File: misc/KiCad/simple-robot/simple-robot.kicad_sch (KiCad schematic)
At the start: 46 parts, among them J1 MotLA, J10 Screw_Terminal_2_P5.00mm, J2 MotLB, J4 MotRA, J5 MotRB, J6 ENC_LF, J7 ENC_LR, J8 ENC_RF, J9 ENC_RR, P1 Port Expander, U1 Pico2

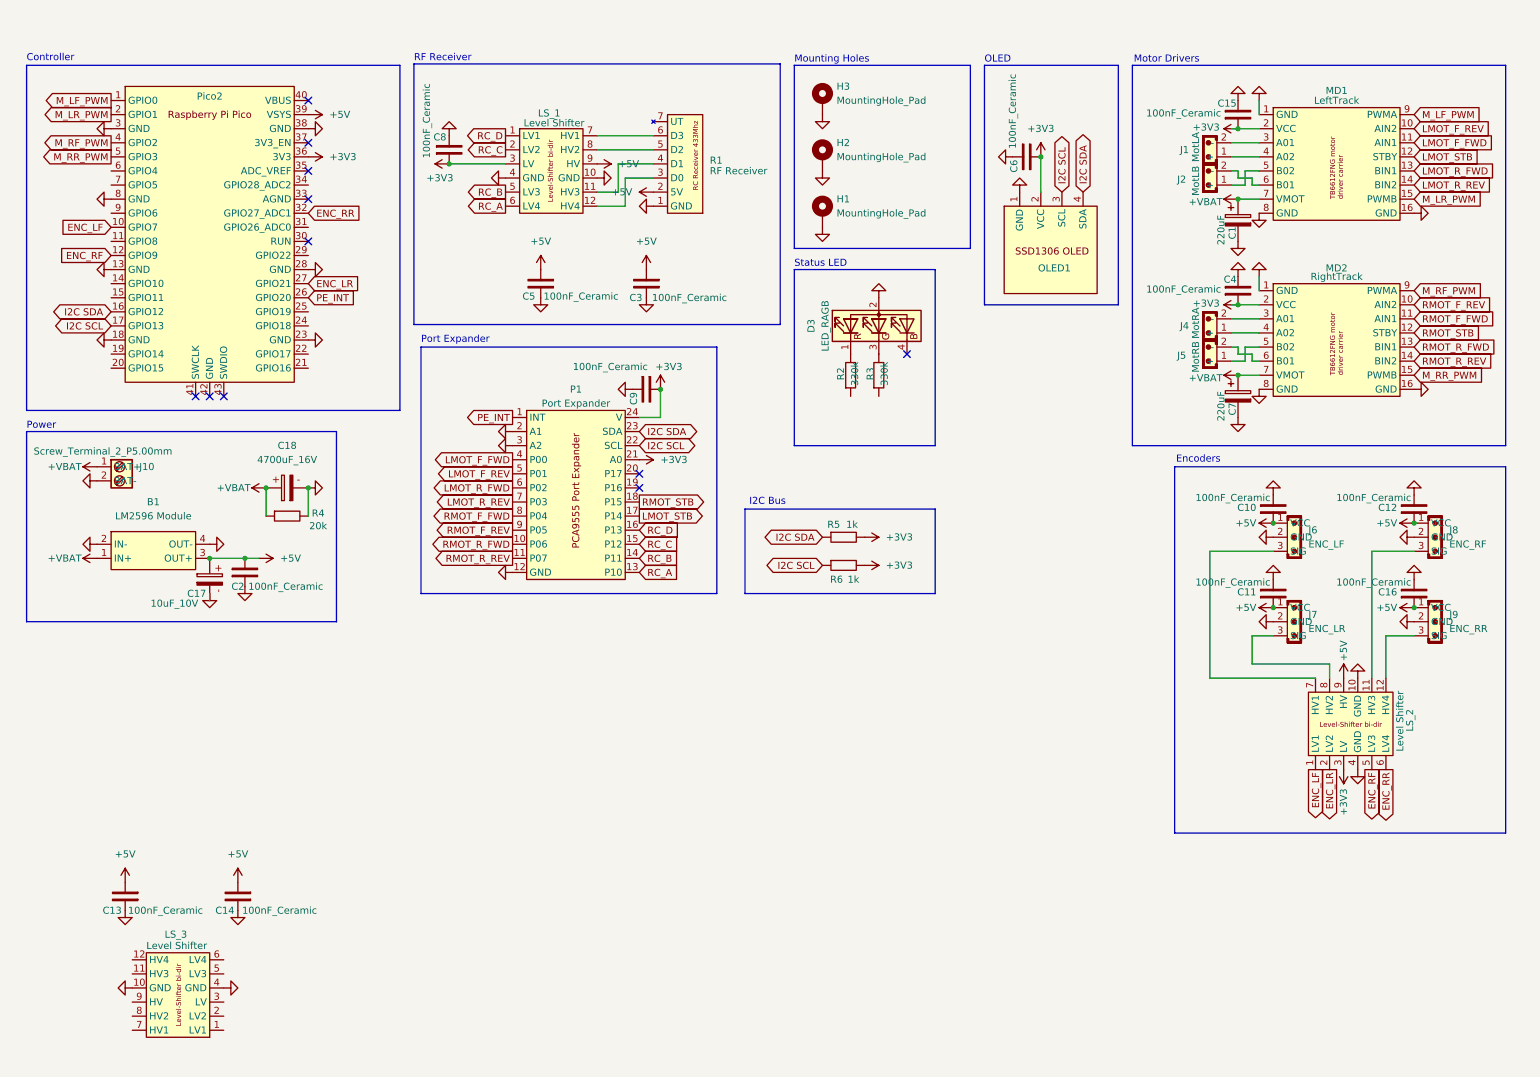
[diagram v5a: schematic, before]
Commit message: Update KiCad schematic to include all connections and IC
Make KiCad PCB 4-layer and update footprints
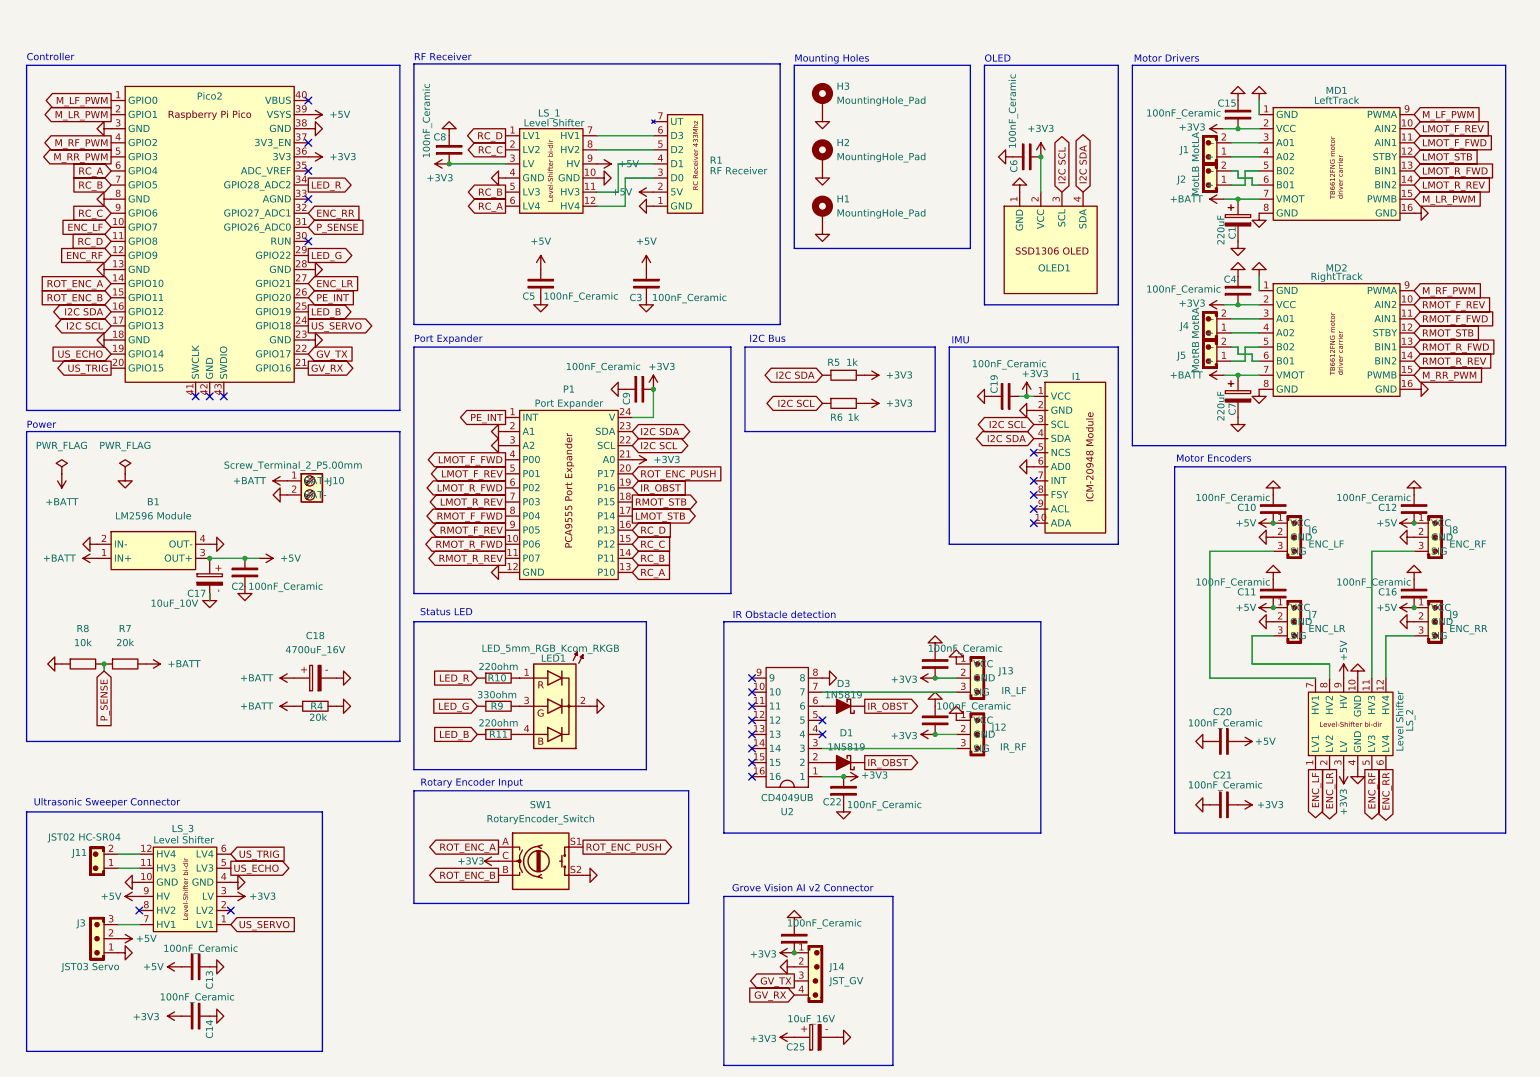
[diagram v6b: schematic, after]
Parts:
- removed D3: LED_RAGB, common-hobby-things:LED RAGB, symbol Device:LED_RAGB
- removed R2, R3: 330k, Resistor_THT:R_Axial_DIN0207_L6.3mm_D2.5mm_P10.16mm_Horizontal, symbol PCM_SL_Resistors:330k
- added C19, C20, C21, C22, C23, C24, C26: 100nF_Ceramic, Capacitor_THT:C_Disc_D5.0mm_W2.5mm_P2.50mm, symbol PCM_SL_Capacitors:100nF_Ceramic
- added C25: 10uF_16V, Capacitor_THT:CP_Radial_D5.0mm_P2.00mm, symbol PCM_SL_Capacitors:10uF_16V
- added D1, D3: 1N5819, PCM_Diode_THT_AKL:D_DO-41_SOD81_P7.62mm_Horizontal, symbol PCM_Diode_Schottky_AKL:1N5819
- added I1: ~, common-hobby-things:ICM-20948-module, symbol common-hobby-things:ICM-20948-module
- added J11: JST02 HC-SR04, Connector_JST:JST_EH_B2B-EH-A_1x02_P2.50mm_Vertical, symbol PCM_SL_Connectors:JST_02
- added J12: IR_RF, Connector_JST:JST_PH_B3B-PH-K_1x03_P2.00mm_Vertical, symbol PCM_SL_Connectors:JST_03
- added J13: IR_LF, Connector_JST:JST_PH_B3B-PH-K_1x03_P2.00mm_Vertical, symbol PCM_SL_Connectors:JST_03
- added J14: JST_GV, Connector_JST:JST_EH_B4B-EH-A_1x04_P2.50mm_Vertical, symbol PCM_SL_Connectors:JST_04
- added J3: JST03 Servo, Connector_JST:JST_EH_B3B-EH-A_1x03_P2.50mm_Vertical, symbol PCM_SL_Connectors:JST_03
- added LED1: LED_5mm_RGB_Kcom_RKGB, PCM_LED_THT_AKL:LED_D5.0mm-4_RGB_Wide_Pins, symbol PCM_LED_AKL:LED_5mm_RGB_Kcom_RKGB
- added R10, R11: 220ohm, Resistor_THT:R_Axial_DIN0207_L6.3mm_D2.5mm_P10.16mm_Horizontal, symbol PCM_SL_Resistors:220ohm
- added R7: 20k, Resistor_THT:R_Axial_DIN0207_L6.3mm_D2.5mm_P10.16mm_Horizontal, symbol PCM_SL_Resistors:20k
- added R8: 10k, Resistor_THT:R_Axial_DIN0207_L6.3mm_D2.5mm_P10.16mm_Horizontal, symbol PCM_SL_Resistors:10k
- added R9: 330ohm, Resistor_THT:R_Axial_DIN0207_L6.3mm_D2.5mm_P10.16mm_Horizontal, symbol PCM_SL_Resistors:330ohm
- added SW1: RotaryEncoder_Switch, Rotary_Encoder:RotaryEncoder_Alps_EC11E-Switch_Vertical_H20mm, symbol Device:RotaryEncoder_Switch
- added U2: CD4049UB, Package_DIP:DIP-16_W7.62mm_LongPads, symbol PCM_SL_Devices:IC_DIP_16
- U1: footprint MCU_RaspberryPi_and_Boards:RPi_Pico_SMD_TH -> PCM_SL_Development_Boards:raspberry_pi_pico_THT
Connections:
- net +3V3: now also C14.1, LS_3.3 (LV), C19.1, C21.2, C22.2, C23.1, C24.1, C25.1, C26.1, I1.1 (VCC), J12.2 (GND), J13.2 (GND), J14.1, SW1.C, U2.1
- net +5V: now also LS_3.9 (HV), C20.2, J3.2; no longer C14.1
- net GND: now also C19.2, C20.1, C21.1, C22.1, C23.2, C24.2, C25.2, C26.2, I1.2 (GND), I1.6 (AD0), J12.1 (VCC), J13.1 (VCC), J14.2, J3.1, LED1.2 (A), R8.1, SW1.S2, U2.8
- net I2C SCL: now also I1.3 (SCL)
- net I2C SDA: now also I1.4 (SDA)
- net RC_A: now also U1.6 (GPIO4)
- net RC_B: now also U1.7 (GPIO5)
- net RC_C: now also U1.9 (GPIO6)
- net RC_D: now also U1.11 (GPIO8)
- net US_SERVO: now reaches LS_3.1 (LV1)
- net US_SERVO: now also U1.24 (GPIO18)
- net at LS_3.11 (HV3): now also J11.1
- net at LS_3.12 (HV4): now also J11.2
- net US_ECHO: now reaches LS_3.5 (LV3)
- net US_ECHO: now also U1.19 (GPIO14)
- net US_TRIG: now reaches LS_3.6 (LV4)
- net US_TRIG: now also U1.20 (GPIO15)
- net at LS_3.7 (HV1): now also J3.3
- net IR_OBST: now reaches P1.19 (P16)
- net IR_OBST: now also D1.1 (K), D3.1 (K)
- net ROT_ENC_PUSH: now reaches P1.20 (P17)
- net ROT_ENC_PUSH: now also SW1.S1
- net ROT_ENC_A: now reaches U1.14 (GPIO10)
- net ROT_ENC_A: now also SW1.A
- net ROT_ENC_B: now reaches U1.15 (GPIO11)
- net ROT_ENC_B: now also SW1.B
- net GV_RX: now reaches U1.21 (GPIO16)
- net GV_RX: now also J14.4
- net GV_TX: now reaches U1.22 (GPIO17)
- net GV_TX: now also J14.3
- net LED_B: now reaches U1.25 (GPIO19)
- net LED_B: now also R11.1
- net LED_G: now reaches U1.29 (GPIO22)
- net LED_G: now also R9.1
- net P_SENSE: now reaches U1.31 (GPIO26_ADC0)
- net P_SENSE: now also R7.1, R8.2
- net LED_R: now reaches U1.34 (GPIO28_ADC2)
- net LED_R: now also R10.1
- net +VBAT renamed +BATT
- net +BATT: now also R7.2
- new net: D1.2 (A), U2.2
- new net: J12.3 (SIG), U2.3
- new net: D3.2 (A), U2.6
- new net: J13.3 (SIG), U2.7
- new net: LED1.3 (G), R9.2
- new net: LED1.1 (R), R10.2
- new net: LED1.4 (B), R11.2
- no-connect marks 11 -> 25
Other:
- note added: "Grove Vision AI v2 Connector"
- note added: "IMU"
- note added: "IR Obstacle detection"
- note added: "Motor Encoders"
- note added: "Rotary Encoder Input"
- note added: "Ultrasonic Sweeper Connector"
- note removed: "Encoders"
- moved on the sheet: C13, C14, C18, C9, J10, LS_3, P1, R4, R5, R6

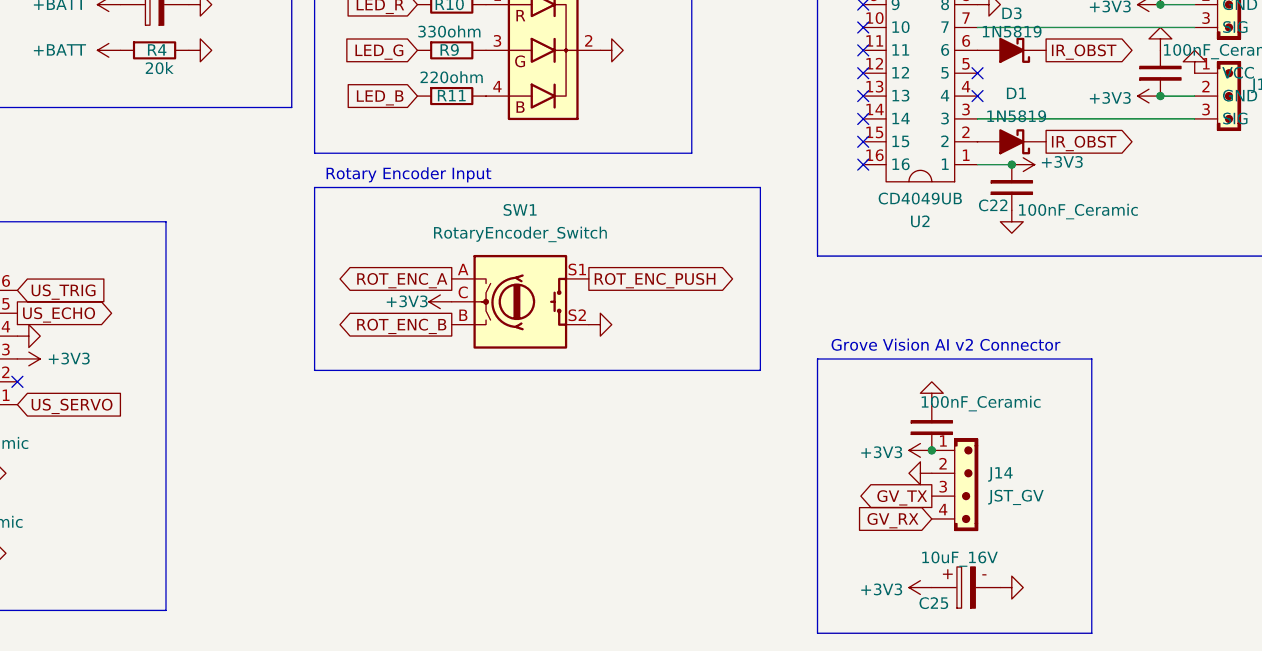
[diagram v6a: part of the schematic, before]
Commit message: Add 47ohm resistor and reposition schematic parts
Add new PCM_SL_Resistors:47ohm symbol and instantiate R3
Reposition rotary encoder, GV_TX/GV_RX and several power/GND
symbols; add short wires and junctions to reconnect traces
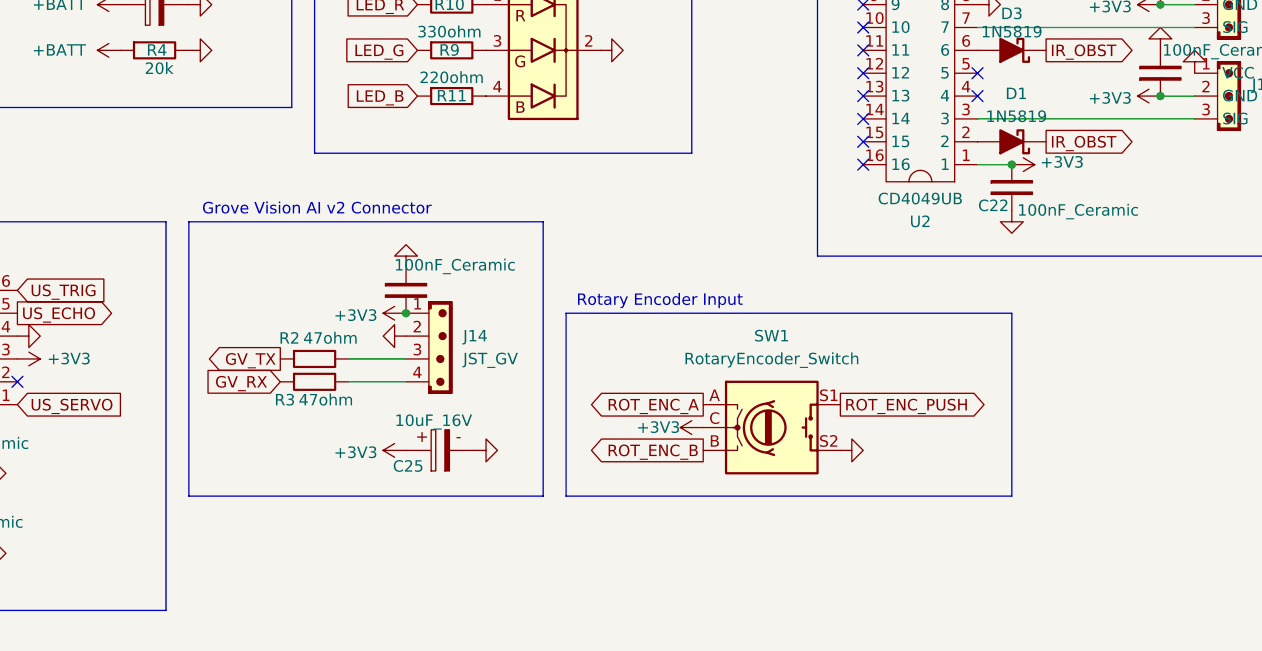
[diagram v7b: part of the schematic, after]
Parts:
- added R2, R3: 47ohm, Resistor_THT:R_Axial_DIN0207_L6.3mm_D2.5mm_P10.16mm_Horizontal, symbol PCM_SL_Resistors:47ohm
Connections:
- net GV_RX: now also R3.1; no longer J14.4
- net GV_TX: now also R2.1; no longer J14.3
- new net: J14.3, R2.2
- new net: J14.4, R3.2
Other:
- moved on the sheet: C25, J14, SW1

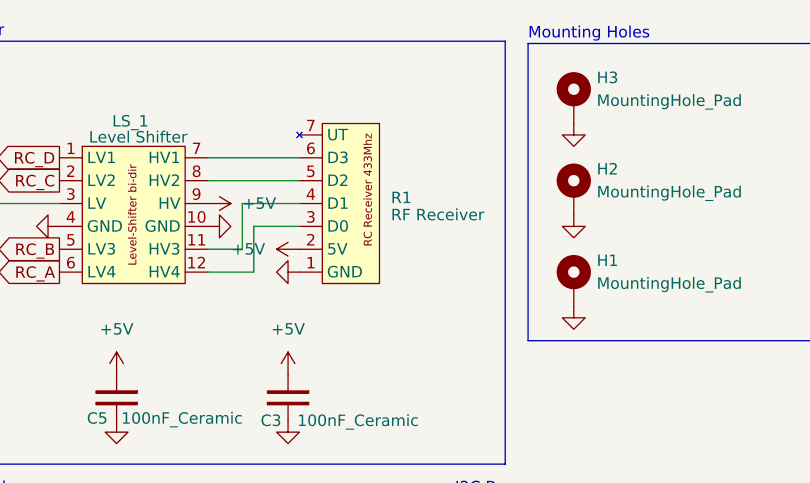
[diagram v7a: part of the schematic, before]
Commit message: Add JST connectors, rename nets, update footprints
Rename power net +VBAT to +BATT and label several previously
unconnected nets (e.g. IR_OBST, GV_TX/GV_RX, Net-(D1-A), Net-(D3-A),
and various Jx pins). Add JST RF_PWR (J16) and RF_Logic (J15)
symbols to the schematic. Replace/adjust footprint and properties for
the capacitor/MD1 component and update reference/value/metadata.
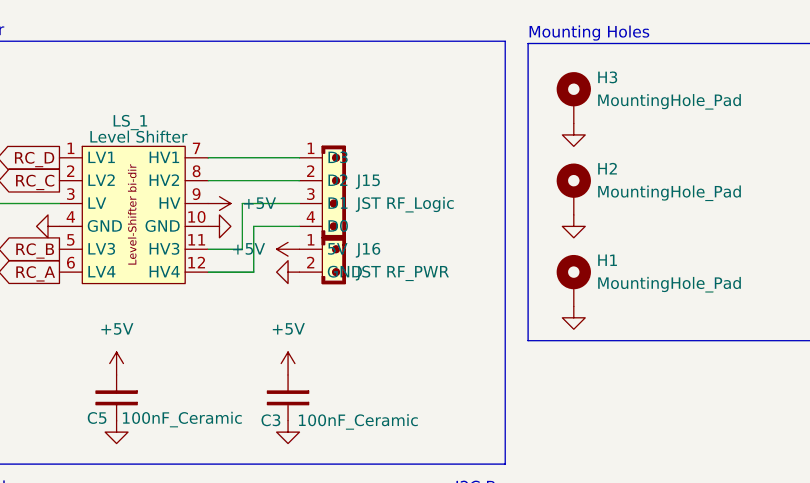
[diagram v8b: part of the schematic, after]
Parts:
- removed R1: RF Receiver, common-hobby-things:433Mhz RC Receiver, symbol common-hobby-things:RC_Receiver
- added J15: JST RF_Logic, Connector_JST:JST_EH_B4B-EH-A_1x04_P2.50mm_Vertical, symbol PCM_SL_Connectors:JST_04
- added J16: JST RF_PWR, Connector_JST:JST_EH_B2B-EH-A_1x02_P2.50mm_Vertical, symbol PCM_SL_Connectors:JST_02
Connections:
- net +5V: now also J16.1 (5V)
- net GND: now also J16.2 (GND)
- net at LS_1.12 (HV4): now also J15.4 (D0)
- net at LS_1.11 (HV3): now also J15.3 (D1)
- net at LS_1.8 (HV2): now also J15.2 (D2)
- net at LS_1.7 (HV1): now also J15.1 (D3)
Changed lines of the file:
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@@
 	)
 	(symbol
+		(lib_name "JST_04_1")
+		(lib_id "PCM_SL_Connectors:JST_04")
+		(at 132.08 33.274 0)
+		(unit 1)
+		(exclude_from_sim no)
+		(in_bom yes)
+		(on_board yes)
+		(dnp no)
+		(fields_autoplaced yes)
+		(property "Reference" "J15"
+			(at 134.62 31.7499 0)
+			(effects
+				(font
+					(size 1.27 1.27)
+				)
+				(justify left)
+			)
+		)
+		(property "Value" "JST RF_Logic"
+			(at 134.62 34.2899 0)
+			(effects
+				(font
+					(size 1.27 1.27)
+				)
+				(justify left)
+			)
+		)
+		(property "Footprint" "Connector_JST:JST_EH_B4B-EH-A_1x04_P2.50mm_Vertical"
+			(at 132.08 24.13 0)
+			(effects
+				(font
+					(size 1.27 1.27)
+				)
+				(hide yes)
+			)
+		)
+		(property "Datasheet" ""
+			(at 132.08 24.13 0)
+			(effects
+				(font
+					(size 1.27 1.27)
+				)
+				(hide yes)
+			)
+		)
+		(property "Description" "JST Connector  4 pins"
+			(at 132.08 33.274 0)
+			(effects
+				(font
+					(size 1.27 1.27)
+				)
+				(hide yes)
+			)
+		)
+		(pin "1"
+		)
+		(pin "4"
+		)
+		(pin "3"
+		)
+		(pin "2"
+		)
+		(instances
+			(project ""
+				(path "/bab01379-5d77-437e-95b1-5e737eb23384"
+					(reference "J15")
+					(unit 1)
+				)
+			)
+		)
+	)
+	(symbol
 		(lib_id "PCM_SL_Connectors:JST_03")
 		(at 186.69 127 0)
@@
 	)
 	(symbol
-		(lib_id "common-hobby-things:RC_Receiver")
-		(at 133.35 44.45 180)
-		(unit 1)
-		(exclude_from_sim no)
-		(in_bom yes)
-		(on_board yes)
-		(dnp no)
-		(fields_autoplaced yes)
-		(property "Reference" "R1"
-			(at 138.43 33.6549 0)
-			(effects
-				(font
-					(size 1.27 1.27)
-				)
-				(justify right)
-			)
-		)
-		(property "Value" "RF Receiver"
-			(at 138.43 35.56 0)
-			(effects
-				(font
-					(size 1.27 1.27)
-				)
-				(justify right)
-			)
-		)
-		(property "Footprint" "common-hobby-things:433Mhz RC Receiver"
-			(at 133.35 44.45 0)
-			(effects
-				(font
-					(size 1.27 1.27)
-				)
-				(hide yes)
-			)
-		)
-		(property "Datasheet" ""
-			(at 133.35 44.45 0)
-			(effects
-				(font
-					(size 1.27 1.27)
-				)
-				(hide yes)
-			)
-		)
-		(property "Description" ""
-			(at 133.35 44.45 0)
-			(effects
-				(font
-					(size 1.27 1.27)
-				)
-				(hide yes)
-			)
-		)
-		(pin "6"
-		)
-		(pin "7"
-		)
-		(pin "4"
-		)
-		(pin "5"
-		)
-		(pin "1"
-		)
-		(pin "2"
-		)
-		(pin "3"
-		)
-		(instances
-			(project ""
-				(path "/bab01379-5d77-437e-95b1-5e737eb23384"
-					(reference "R1")
-					(unit 1)
-				)
-			)
-		)
-	)
-	(symbol
 		(lib_id "power:+3V3")
 		(at 231.14 27.94 90)
@@
 					(unit 1)
 				)
+			)
+		)
+	)
+	(symbol
+		(lib_name "JST_02_2")
+		(lib_id "PCM_SL_Connectors:JST_02")
+		(at 132.08 40.64 0)
+		(unit 1)
+		(exclude_from_sim no)
+		(in_bom yes)
+		(on_board yes)
+		(dnp no)
+		(fields_autoplaced yes)
+		(property "Reference" "J16"
+			(at 134.62 39.3699 0)
+			(effects
+				(font
+					(size 1.27 1.27)
+				)
+				(justify left)
+			)
+		)
+		(property "Value" "JST RF_PWR"
+			(at 134.62 41.9099 0)
+			(effects
+				(font
+					(size 1.27 1.27)
+				)
+				(justify left)
+			)
+		)
+		(property "Footprint" "Connector_JST:JST_EH_B2B-EH-A_1x02_P2.50mm_Vertical"
+			(at 132.08 34.29 0)
+			(effects
+				(font
+					(size 1.27 1.27)
+				)
+				(hide yes)
+			)
+		)
+		(property "Datasheet" ""
+			(at 132.08 34.29 0)
+			(effects
+				(font
+					(size 1.27 1.27)
+				)
+				(hide yes)
+			)
+		)
+		(property "Description" "JST Connector  2 pins"
+			(at 132.08 40.64 0)
+			(effects
+				(font
+					(size 1.27 1.27)
+				)
+				(hide yes)
+			)
+		)
+		(pin "2"
+		)
+		(pin "1"
+		)
+		(instances
+			(project ""
+				(path "/bab01379-5d77-437e-95b1-5e737eb23384"
+					(reference "J16")
+					(unit 1)
+				)
